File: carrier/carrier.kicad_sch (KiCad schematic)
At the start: 0 parts

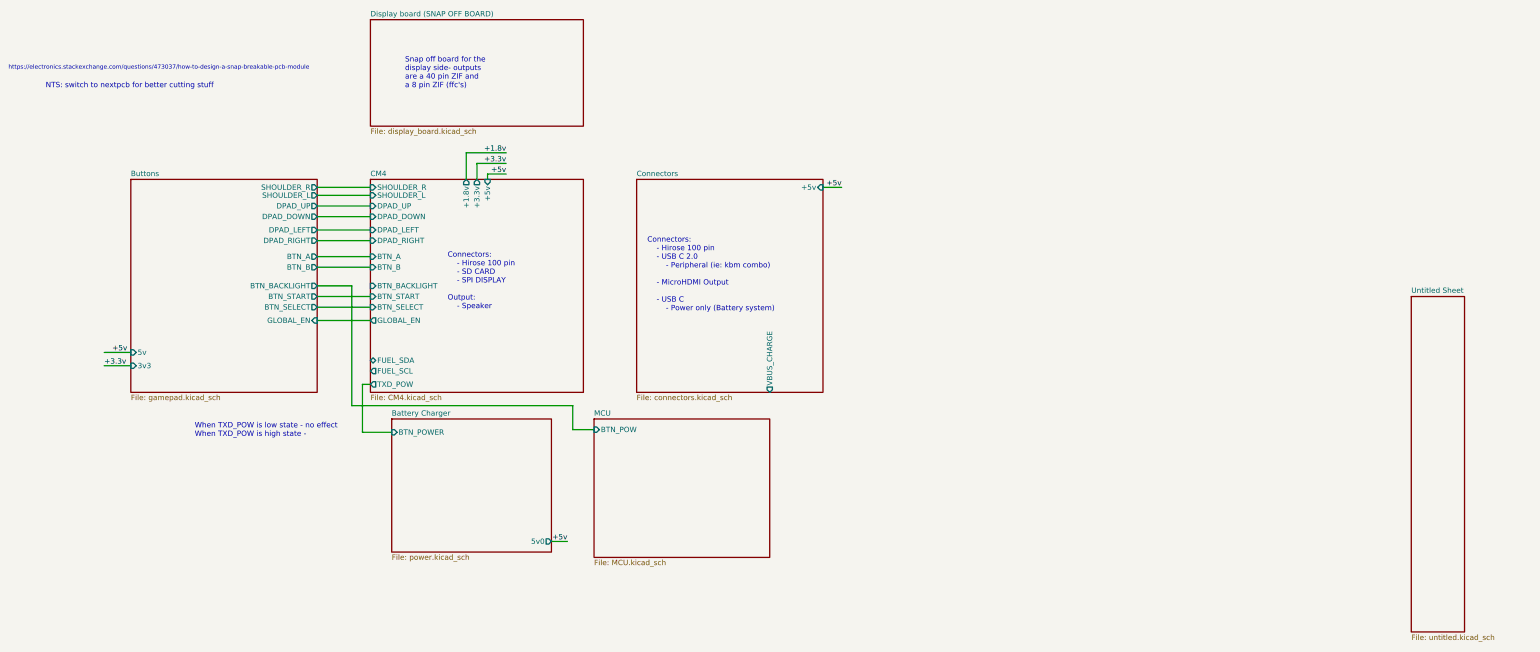
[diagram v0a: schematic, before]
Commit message: fixed switching and added fuel gague
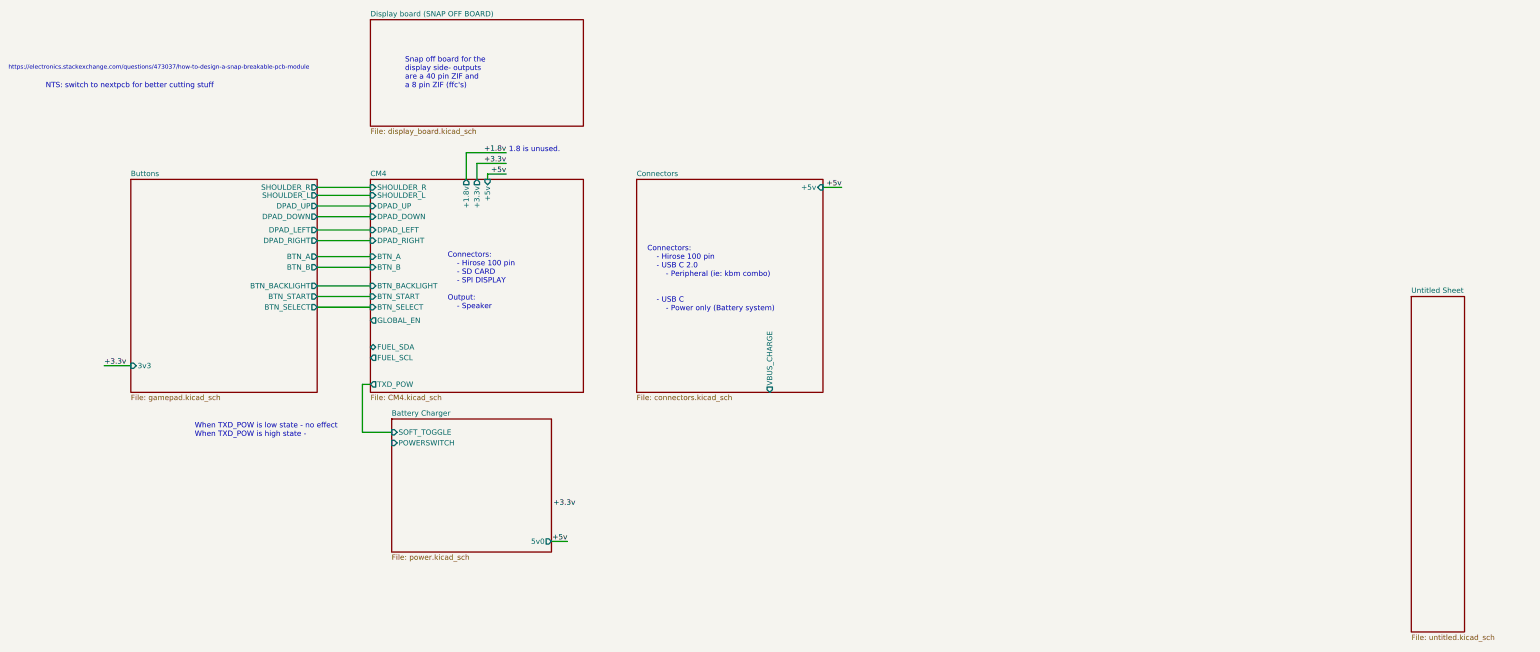
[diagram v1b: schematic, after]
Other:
- removed sheet MCU
- sheet Battery Charger ports: added POWERSWITCH, SOFT_TOGGLE; removed BTN_POWER
- sheet Buttons ports: added none; removed 5v, GLOBAL_EN
- note added: "1.8 is unused."
- note added: "Connectors: - Hirose 100 pin - USB C 2.0 - Peripheral (ie: kbm combo) - USB C - Power only (Battery system)"
- note removed: "Connectors: - Hirose 100 pin - USB C 2.0 - Peripheral (ie: kbm combo) - MicroHDMI Output - USB C - Power only (Battery system)"

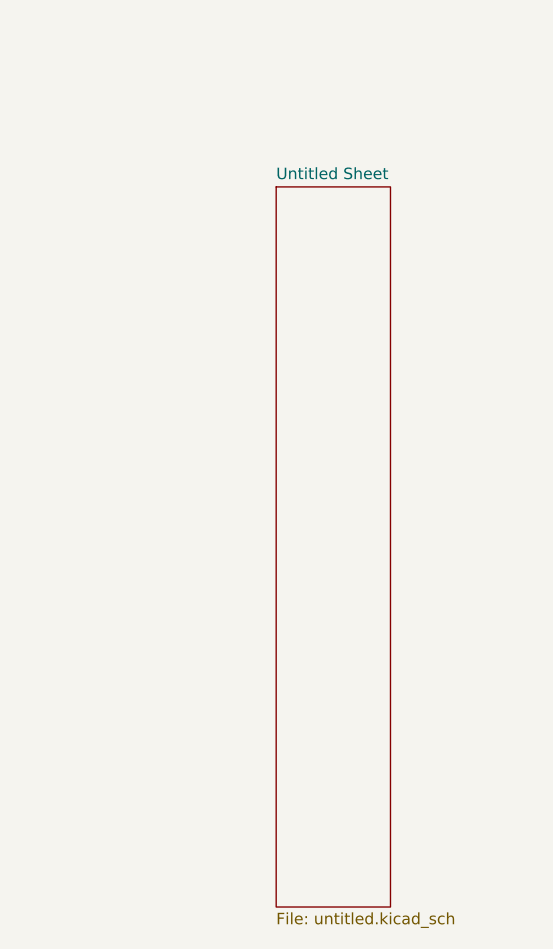
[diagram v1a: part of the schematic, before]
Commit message: need to finish footprint assignments then can do rev2 pcb (cooler one)
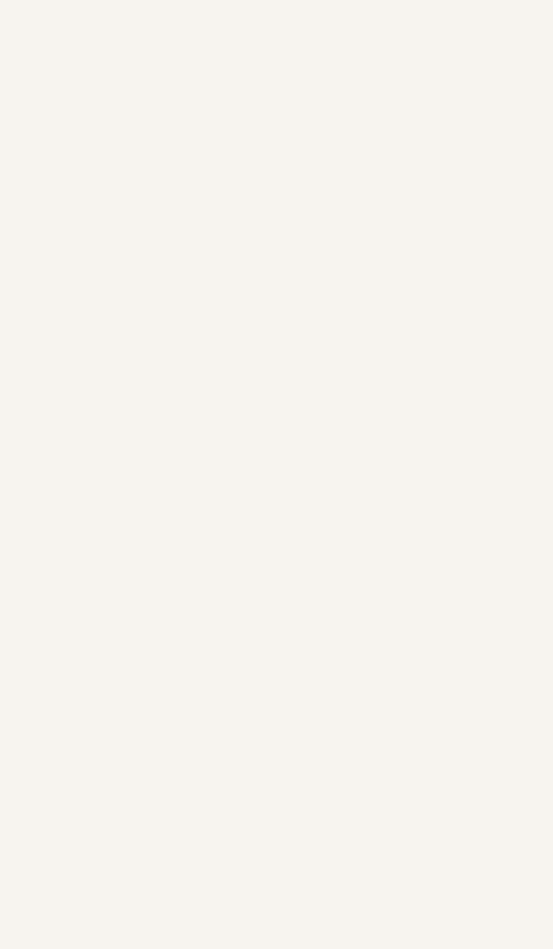
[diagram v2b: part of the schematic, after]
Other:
- removed sheet Untitled Sheet
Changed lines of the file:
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@@
+    (stroke (width 0) (type solid) (color 0 0 0 0))
+  )
+  (wire (pts (xy 159.385 53.34) (xy 152.4 53.34))
     (stroke (width 0) (type solid) (color 0 0 0 0))
   )
@@
     (stroke (width 0) (type solid) (color 0 0 0 0))
   )
-  (wire (pts (xy 159.385 53.34) (xy 152.4 53.34))
-    (stroke (width 0) (type solid) (color 0 0 0 0))
-  )
   (wire (pts (xy 114.3 63.5) (xy 127 63.5))
     (stroke (width 0) (type solid) (color 0 0 0 0))
   )
+  (wire (pts (xy 159.385 50.8) (xy 149.86 50.8))
+    (stroke (width 0) (type solid) (color 0 0 0 0))
+  )
   (wire (pts (xy 149.86 50.8) (xy 149.86 57.15))
-    (stroke (width 0) (type solid) (color 0 0 0 0))
-  )
-  (wire (pts (xy 159.385 50.8) (xy 149.86 50.8))
     (stroke (width 0) (type solid) (color 0 0 0 0))
   )
@@
   (label "+1.8v" (at 159.385 50.8 180)
     (effects (font (size 1.27 1.27)) (justify right bottom))
-  )
-  (sheet (at 375.285 85.09) (size 12.7 80.01) (fields_autoplaced)
-    (stroke (width 0.1524) (type solid) (color 0 0 0 0))
-    (fill (color 0 0 0 0.0000))
-    (property "Sheet name" "Untitled Sheet" (id 0) (at 375.285 84.3784 0)
-      (effects (font (size 1.27 1.27)) (justify left bottom))
-    )
-    (property "Sheet file" "untitled.kicad_sch" (id 1) (at 375.285 165.6846 0)
-      (effects (font (size 1.27 1.27)) (justify left top))
-    )
   )
   (sheet (at 127 57.15) (size 50.8 50.8) (fields_autoplaced)
@@
     (path "/7d2c72bb-6811-42b4-a3fa-d7ba2c227aca" (page "5"))
     (path "/95ef1699-d890-4da8-941a-b0ab341c2e25" (page "6"))
-    (path "/114b5e56-0032-45d3-b5fa-4bcf49f0b464" (page "8"))
   )
   (symbol_instances
@@
       (reference "#PWR06") (unit 1) (value "GND") (footprint "")
     )
-    (path "/19c5e008-dc4a-4080-a2ed-5cdad03792a4/efd75527-30b9-4346-9c4d-77e3ec0eec03"
-      (reference "#PWR07") (unit 1) (value "GND") (footprint "")
-    )
     (path "/19c5e008-dc4a-4080-a2ed-5cdad03792a4/b2d459b2-8ee3-44bc-b145-b0f79fbcb7e7"
       (reference "#PWR08") (unit 1) (value "GND") (footprint "")
@@
       (reference "#PWR045") (unit 1) (value "GND1") (footprint "")
     )
-    (path "/114b5e56-0032-45d3-b5fa-4bcf49f0b464/7b653641-f125-4a83-9d0d-9bef26942a73"
-      (reference "#PWR046") (unit 1) (value "GND") (footprint "")
-    )
-    (path "/114b5e56-0032-45d3-b5fa-4bcf49f0b464/7af4f7d6-f443-4ace-a1a0-7f5aa0b61317"
-      (reference "#PWR047") (unit 1) (value "GND") (footprint "")
+    (path "/19c5e008-dc4a-4080-a2ed-5cdad03792a4/d8d1afed-4cde-4555-a277-aa16b2f1bd05"
+      (reference "#PWR?") (unit 1) (value "GND") (footprint "")
     )
     (path "/19c5e008-dc4a-4080-a2ed-5cdad03792a4/8818e57c-5f66-4d5d-9da6-2a6e75c0d509"
@@
       (reference "C25") (unit 1) (value "1u") (footprint "")
     )
-    (path "/114b5e56-0032-45d3-b5fa-4bcf49f0b464/b3393a8c-5899-4c2d-a7a3-bde747eaffc1"
-      (reference "C26") (unit 1) (value "22u") (footprint "")
-    )
     (path "/19c5e008-dc4a-4080-a2ed-5cdad03792a4/86f057dd-5f37-4747-a676-a365d3666b91"
       (reference "D1") (unit 1) (value "LED") (footprint "LED_SMD:LED_0805_2012Metric_Pad1.15x1.40mm_HandSolder")
@@
     )
     (path "/8d0ae364-2b30-4b7c-813a-81b59cbe3cd0/13e5f360-e05a-4fcd-8f19-b3b45d4a5e31"
-      (reference "D4") (unit 1) (value "D_Schottky") (footprint "")
+      (reference "D4") (unit 1) (value "D_Schottky") (footprint "Package_TO_SOT_SMD:TO-252-2")
     )
     (path "/8d0ae364-2b30-4b7c-813a-81b59cbe3cd0/d4fff6a7-8bc9-41a0-b5db-336e81252722"
@@
       (reference "D7") (unit 1) (value "8240119") (footprint "CM4IO:SOT143-4L")
     )
-    (path "/19c5e008-dc4a-4080-a2ed-5cdad03792a4/7cba3bcc-f27c-4d98-a241-48d250d0f938"
-      (reference "J1") (unit 1) (value "AudioJack3_Switch") (footprint "audio:audio")
-    )
     (path "/19c5e008-dc4a-4080-a2ed-5cdad03792a4/8e422c52-adbe-4171-a205-d76d513cf48c"
       (reference "J2") (unit 1) (value "52271-0879") (footprint "MOLEXZIF:Molex-52271-0879-Manufacturer_Recommended")
     )
     (path "/19c5e008-dc4a-4080-a2ed-5cdad03792a4/f8140666-196c-4d86-b050-be894d86e98b"
-      (reference "J3") (unit 1) (value "Micro_SD_Card") (footprint "sdcard:HRS_DM3CS-SF")
+      (reference "J3") (unit 1) (value "Micro_SD_Card") (footprint "sdcard:GCT_MEM2067-02-180-00-A_REVB")
     )
     (path "/8d0ae364-2b30-4b7c-813a-81b59cbe3cd0/1a1d6983-2644-479e-bb31-805e03288d13"
@@
       (reference "J7") (unit 1) (value "52271-0879") (footprint "MOLEXZIF:Molex-52271-0879-Manufacturer_Recommended")
     )
+    (path "/19c5e008-dc4a-4080-a2ed-5cdad03792a4/5d8666c8-65e8-4fca-82d3-8c0a2c793f51"
+      (reference "J?") (unit 1) (value "AudioJack3_Ground_SwitchTR") (footprint "audio:CUI-SJ-43515TS-SMT-TR-0")
+    )
     (path "/8d0ae364-2b30-4b7c-813a-81b59cbe3cd0/91144326-eb9f-4394-a1f2-08503a52a00b"
-      (reference "L1") (unit 1) (value "1uH") (footprint "")
+      (reference "L1") (unit 1) (value "1uH") (footprint "Inductor_SMD:L_Sumida_CDMC6D28_7.25x6.5mm")
     )
     (path "/19c5e008-dc4a-4080-a2ed-5cdad03792a4/62393b50-5922-4171-b75b-ac60ba09522e"
@@
       (reference "Q1") (unit 1) (value "2N2219") (footprint "Package_TO_SOT_THT:TO-39-3")
     )
-    (path "/114b5e56-0032-45d3-b5fa-4bcf49f0b464/8ed212d0-66c8-493e-9ede-e01574dacca2"
-      (reference "Q2") (unit 1) (value "IRF9540N") (footprint "Package_TO_SOT_THT:TO-220-3_Vertical")
-    )
-    (path "/114b5e56-0032-45d3-b5fa-4bcf49f0b464/ab0453a3-0e0d-4ec2-a2d5-b84bbc6944ac"
-      (reference "Q3") (unit 1) (value "2N3904") (footprint "Package_TO_SOT_THT:TO-92_Inline")
-    )
-    (path "/114b5e56-0032-45d3-b5fa-4bcf49f0b464/93271846-f4bb-485d-8fb4-263ff3267c06"
-      (reference "Q4") (unit 1) (value "2N3904") (footprint "Package_TO_SOT_THT:TO-92_Inline")
-    )
     (path "/19c5e008-dc4a-4080-a2ed-5cdad03792a4/06e70f63-2271-4617-996d-cb617e89427d"
       (reference "R1") (unit 1) (value "220") (footprint "Resistor_SMD:R_0402_1005Metric_Pad0.72x0.64mm_HandSolder")
@@
       (reference "R6") (unit 1) (value "150") (footprint "Resistor_SMD:R_0603_1608Metric_Pad0.98x0.95mm_HandSolder")
     )
-    (path "/19c5e008-dc4a-4080-a2ed-5cdad03792a4/1fe5e6fc-d8ab-40b1-bb57-41eaba41ba34"
-      (reference "R7") (unit 1) (value "1M") (footprint "")
-    )
     (path "/19c5e008-dc4a-4080-a2ed-5cdad03792a4/8161c783-499d-4297-96b1-318eca1416ff"
       (reference "R8") (unit 1) (value "15k") (footprint "")
@@
       (reference "R48") (unit 1) (value "33") (footprint "Resistor_SMD:R_0805_2012Metric_Pad1.20x1.40mm_HandSolder")
     )
-    (path "/114b5e56-0032-45d3-b5fa-4bcf49f0b464/048d50de-d13f-4143-a840-a94d8eb8caf4"
-      (reference "R49") (unit 1) (value "100k") (footprint "")
-    )
-    (path "/114b5e56-0032-45d3-b5fa-4bcf49f0b464/cdcec9b4-e4e5-40f0-95d4-4f91f378a998"
-      (reference "R50") (unit 1) (value "100k") (footprint "")
-    )
-    (path "/114b5e56-0032-45d3-b5fa-4bcf49f0b464/297fbc17-b634-4c3c-9b9d-82a3586c9785"
-      (reference "R51") (unit 1) (value "1M") (footprint "")
-    )
-    (path "/114b5e56-0032-45d3-b5fa-4bcf49f0b464/1a8dfff3-13ea-4ad8-b00c-e955fdb922c7"
-      (reference "R52") (unit 1) (value "100k") (footprint "")
-    )
     (path "/19c5e008-dc4a-4080-a2ed-5cdad03792a4/8202608e-6e99-405f-8229-c953d27f956a"
       (reference "SW1") (unit 1) (value "SW_Push") (footprint "")
@@
       (reference "SW13") (unit 1) (value "CSS_1300MC") (footprint "")
     )
-    (path "/114b5e56-0032-45d3-b5fa-4bcf49f0b464/93d1b5e7-ecb7-407b-8c65-02d8a6dff542"
-      (reference "SW14") (unit 1) (value "CSS_1300MC") (footprint "")
-    )
     (path "/19c5e008-dc4a-4080-a2ed-5cdad03792a4/fac91ddb-ee6e-4769-85fa-d6b66dee3232"

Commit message: chrgere
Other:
- sheet Battery Charger ports: added CC1, CC2, DN, DP, VBUS; removed none
- sheet Connectors ports: added pwr_CC1, pwr_CC2, pwr_DN, pwr_DP; removed none
- note added: "USB Connection is CHARGER (CC & BC12. det.)"
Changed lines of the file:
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@@
     (stroke (width 0) (type solid) (color 0 0 0 0))
+  )
+  (wire (pts (xy 190.5 97.155) (xy 182.88 97.155))
+    (stroke (width 0) (type default) (color 0 0 0 0))
+  )
+  (wire (pts (xy 170.18 123.825) (xy 182.88 123.825))
+    (stroke (width 0) (type default) (color 0 0 0 0))
+  )
+  (wire (pts (xy 182.88 97.155) (xy 182.88 123.825))
+    (stroke (width 0) (type default) (color 0 0 0 0))
   )
   (wire (pts (xy 114.3 82.55) (xy 127 82.55))
@@
     (stroke (width 0) (type solid) (color 0 0 0 0))
   )
+  (wire (pts (xy 190.5 92.075) (xy 180.34 92.075))
+    (stroke (width 0) (type default) (color 0 0 0 0))
+  )
+  (wire (pts (xy 180.34 92.075) (xy 180.34 117.475))
+    (stroke (width 0) (type default) (color 0 0 0 0))
+  )
+  (wire (pts (xy 180.34 117.475) (xy 170.18 117.475))
+    (stroke (width 0) (type default) (color 0 0 0 0))
+  )
   (wire (pts (xy 114.3 75.565) (xy 127 75.565))
     (stroke (width 0) (type solid) (color 0 0 0 0))
   )
+  (wire (pts (xy 190.5 101.6) (xy 185.42 101.6))
+    (stroke (width 0) (type default) (color 0 0 0 0))
+  )
+  (wire (pts (xy 185.42 101.6) (xy 185.42 130.175))
+    (stroke (width 0) (type default) (color 0 0 0 0))
+  )
+  (wire (pts (xy 185.42 130.175) (xy 170.18 130.175))
+    (stroke (width 0) (type default) (color 0 0 0 0))
+  )
   (wire (pts (xy 114.3 69.215) (xy 127 69.215))
     (stroke (width 0) (type solid) (color 0 0 0 0))
@@
     (stroke (width 0) (type solid) (color 0 0 0 0))
   )
+  (wire (pts (xy 181.61 95.25) (xy 190.5 95.25))
+    (stroke (width 0) (type default) (color 0 0 0 0))
+  )
+  (wire (pts (xy 170.18 121.92) (xy 181.61 121.92))
+    (stroke (width 0) (type default) (color 0 0 0 0))
+  )
+  (wire (pts (xy 181.61 121.92) (xy 181.61 95.25))
+    (stroke (width 0) (type default) (color 0 0 0 0))
+  )
   (wire (pts (xy 170.18 143.51) (xy 173.99 143.51))
     (stroke (width 0) (type solid) (color 0 0 0 0))
@@
   )
   (wire (pts (xy 125.095 117.475) (xy 132.08 117.475))
+    (stroke (width 0) (type default) (color 0 0 0 0))
+  )
+  (wire (pts (xy 184.15 99.695) (xy 190.5 99.695))
+    (stroke (width 0) (type default) (color 0 0 0 0))
+  )
+  (wire (pts (xy 170.18 128.27) (xy 184.15 128.27))
+    (stroke (width 0) (type default) (color 0 0 0 0))
+  )
+  (wire (pts (xy 184.15 128.27) (xy 184.15 99.695))
     (stroke (width 0) (type default) (color 0 0 0 0))
   )
@@
   )
   (text "NTS: switch to nextpcb for better cutting stuff\n" (at 49.53 35.56 0)
+    (effects (font (size 1.27 1.27)) (justify left bottom))
+  )
+  (text "USB Connection is CHARGER (CC & BC12. det.)\n" (at 170.815 132.715 0)
     (effects (font (size 1.27 1.27)) (justify left bottom))
   )
@@
       (effects (font (size 1.27 1.27)) (justify left top))
     )
-    (pin "VBUS_CHARGE" output (at 222.25 107.95 270)
+    (pin "VBUS_CHARGE" output (at 190.5 92.075 180)
       (effects (font (size 1.27 1.27)) (justify left))
     )
     (pin "+5v" input (at 234.95 59.055 0)
       (effects (font (size 1.27 1.27)) (justify right))
+    )
+    (pin "pwr_CC2" bidirectional (at 190.5 101.6 180)
+      (effects (font (size 1.27 1.27)) (justify left))
+    )
+    (pin "pwr_CC1" bidirectional (at 190.5 99.695 180)
+      (effects (font (size 1.27 1.27)) (justify left))
+    )
+    (pin "pwr_DN" bidirectional (at 190.5 97.155 180)
+      (effects (font (size 1.27 1.27)) (justify left))
+    )
+    (pin "pwr_DP" bidirectional (at 190.5 95.25 180)
+      (effects (font (size 1.27 1.27)) (justify left))
     )
   )
@@
     (pin "POWERSWITCH" input (at 132.08 120.015 180)
       (effects (font (size 1.27 1.27)) (justify left))
+    )
+    (pin "CC1" bidirectional (at 170.18 128.27 0)
+      (effects (font (size 1.27 1.27)) (justify right))
+    )
+    (pin "DN" bidirectional (at 170.18 123.825 0)
+      (effects (font (size 1.27 1.27)) (justify right))
+    )
+    (pin "CC2" bidirectional (at 170.18 130.175 0)
+      (effects (font (size 1.27 1.27)) (justify right))
+    )
+    (pin "DP" bidirectional (at 170.18 121.92 0)
+      (effects (font (size 1.27 1.27)) (justify right))
+    )
+    (pin "VBUS" input (at 170.18 117.475 0)
+      (effects (font (size 1.27 1.27)) (justify right))
     )
   )
@@
       (reference "#PWR034") (unit 1) (value "GND") (footprint "")
     )
-    (path "/8d0ae364-2b30-4b7c-813a-81b59cbe3cd0/cc3137a0-47d5-4926-945a-a2fa17fb60bd"
-      (reference "#PWR035") (unit 1) (value "GND") (footprint "")
-    )
     (path "/8d0ae364-2b30-4b7c-813a-81b59cbe3cd0/aabed5c8-9b01-4a9e-b2ae-66bc604dae59"
       (reference "#PWR036") (unit 1) (value "GND") (footprint "")
@@
       (reference "#PWR045") (unit 1) (value "GND1") (footprint "")
     )
+    (path "/8d0ae364-2b30-4b7c-813a-81b59cbe3cd0/0b37c538-06f2-467b-94a8-863d49bde79e"
+      (reference "#PWR?") (unit 1) (value "GND") (footprint "")
+    )
+    (path "/8d0ae364-2b30-4b7c-813a-81b59cbe3cd0/175220ee-5897-44b6-b7cb-bc6e99dff638"
+      (reference "#PWR?") (unit 1) (value "GND") (footprint "")
+    )
     (path "/8d0ae364-2b30-4b7c-813a-81b59cbe3cd0/24f853a9-cbd0-4d28-9112-c400cd23f3be"
       (reference "#PWR?") (unit 1) (value "GND") (footprint "")
@@
       (reference "C25") (unit 1) (value "1u") (footprint "")
     )
+    (path "/8d0ae364-2b30-4b7c-813a-81b59cbe3cd0/bf5ce354-8542-403d-9704-22e6b67744d6"
+      (reference "C?") (unit 1) (value "10u") (footprint "")
+    )
     (path "/8d0ae364-2b30-4b7c-813a-81b59cbe3cd0/fc6c0b01-a5a5-4efc-987f-5817cb208550"
       (reference "C?") (unit 1) (value "470n") (footprint "")
@@
       (reference "D6") (unit 1) (value "8240116") (footprint "Package_TO_SOT_SMD:SOT-143R_Reverse_Handsoldering")
     )
+    (path "/8d0ae364-2b30-4b7c-813a-81b59cbe3cd0/2cb12f1e-cbd0-460f-aabc-9bd9c9039ac3"
+      (reference "D?") (unit 1) (value "LED") (footprint "")
+    )
+    (path "/8d0ae364-2b30-4b7c-813a-81b59cbe3cd0/e1c82d09-de82-4a9f-99d0-1f415ece7e35"
+      (reference "D?") (unit 1) (value "LED") (footprint "")
+    )
     (path "/19c5e008-dc4a-4080-a2ed-5cdad03792a4/5d8666c8-65e8-4fca-82d3-8c0a2c793f51"
       (reference "J1") (unit 1) (value "AudioJack3_Ground_SwitchTR") (footprint "audio:CUI-SJ-43515TS-SMT-TR-0")
@@
       (reference "R47") (unit 1) (value "33") (footprint "Resistor_SMD:R_0805_2012Metric_Pad1.20x1.40mm_HandSolder")
     )
+    (path "/8d0ae364-2b30-4b7c-813a-81b59cbe3cd0/6e3b1e51-4285-400d-971a-4c11db7a6b80"
+      (reference "R?") (unit 1) (value "R") (footprint "")
+    )
+    (path "/8d0ae364-2b30-4b7c-813a-81b59cbe3cd0/a242d8b3-dadf-4660-8e88-c3ae7d4ccb48"
+      (reference "R?") (unit 1) (value "R") (footprint "")
+    )
     (path "/19c5e008-dc4a-4080-a2ed-5cdad03792a4/8202608e-6e99-405f-8229-c953d27f956a"
